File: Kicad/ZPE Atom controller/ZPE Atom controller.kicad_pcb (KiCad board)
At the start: 2 copper layers, 160 x 71.1 mm, 22 parts, among them IC1 TC4424AVPA, P1 CONN_01X18, P2 CONN_01X18, Q1 PN2222A, T1 Transformer_SP_1S, U1 SSD1306, U2 LM7805_TO220

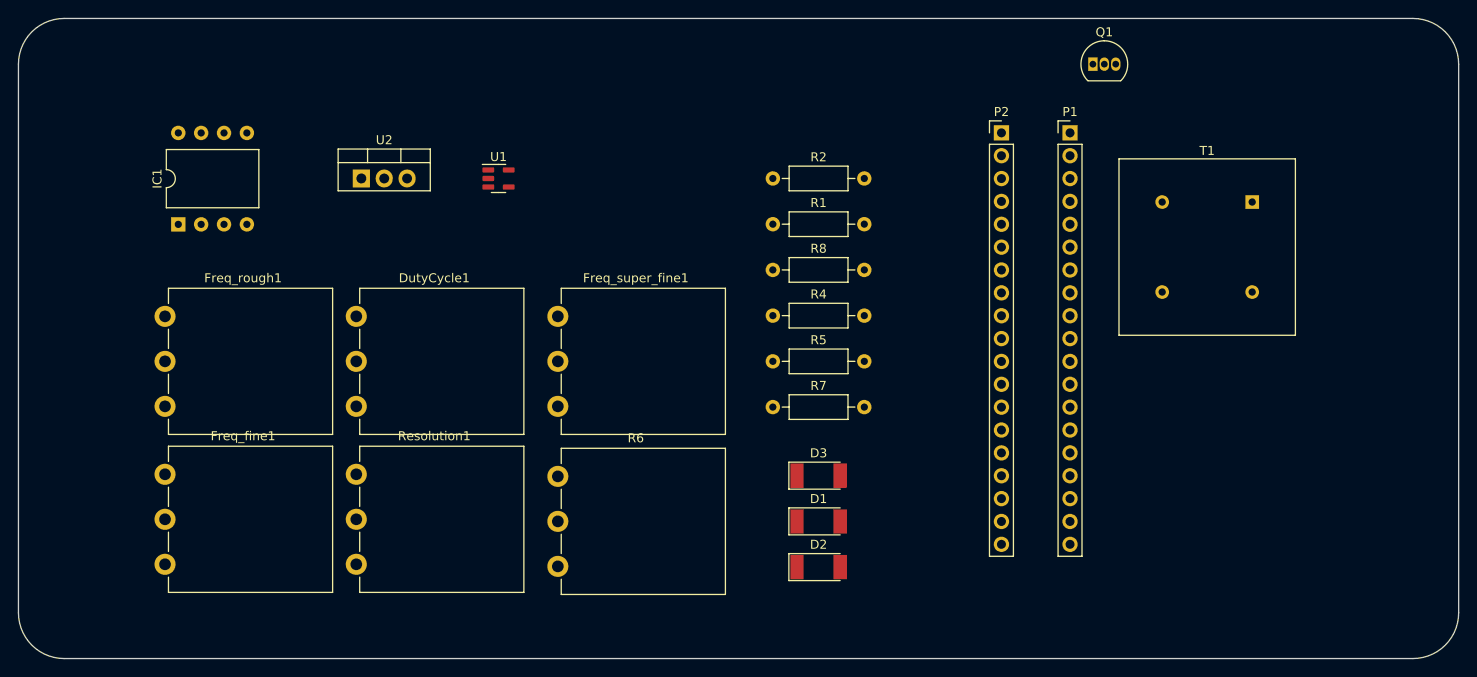
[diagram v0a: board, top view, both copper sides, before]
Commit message: Added AC level convert on inputs
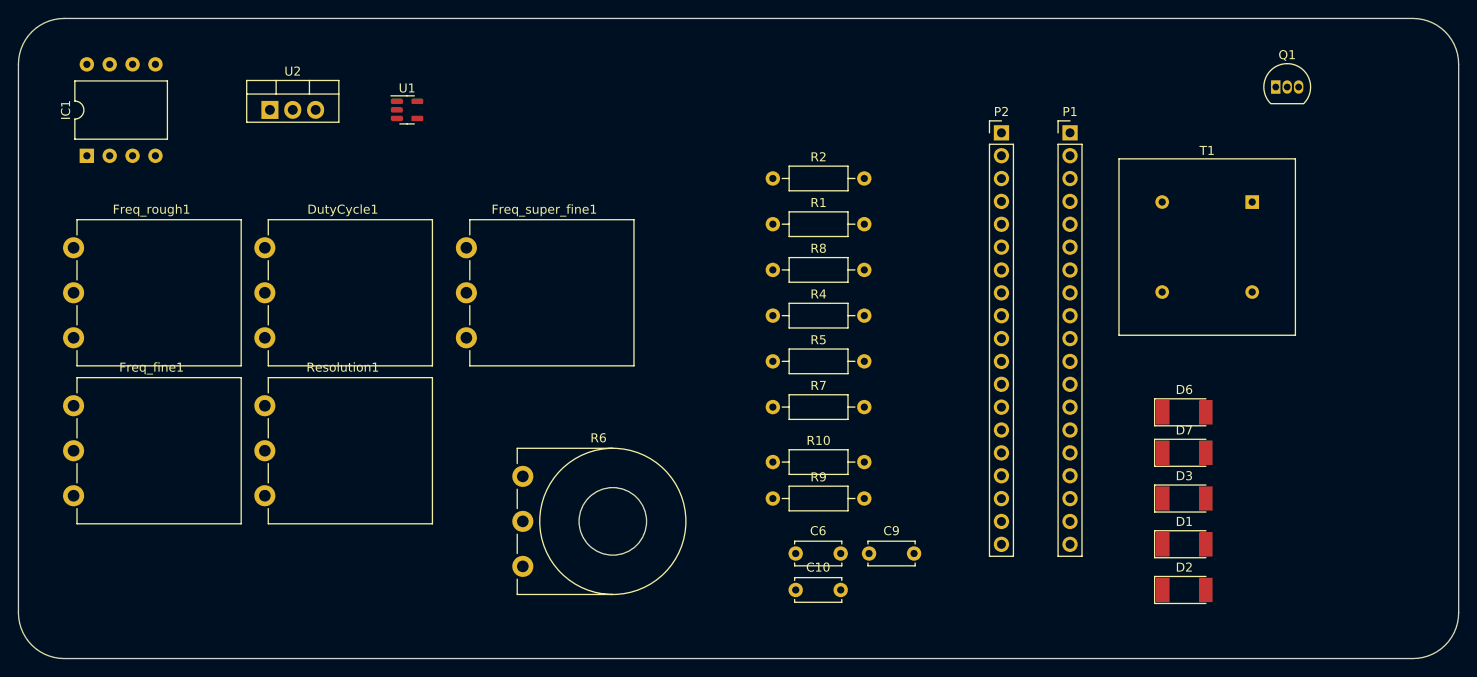
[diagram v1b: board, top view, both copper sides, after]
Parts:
- added C10: 10nF, Capacitor_THT:C_Disc_D5.0mm_W2.5mm_P5.00mm, F.Cu at (154.9, 124.5)
- added C6: 1NF 400V, Capacitor_THT:C_Disc_D5.0mm_W2.5mm_P5.00mm, F.Cu at (154.9, 120.4)
- added C9: 10nF, Capacitor_THT:C_Disc_D5.0mm_W2.5mm_P5.00mm, F.Cu at (163.1, 120.4)
- added D6: 4004, Diode_SMD:D_MELF, F.Cu at (198.1, 104.7)
- added D7: 4004, Diode_SMD:D_MELF, F.Cu at (198.1, 109.2)
- added R10: 1M, Resistor_THT:R_Axial_DIN0207_L6.3mm_D2.5mm_P10.16mm_Horizontal, F.Cu at (152.4, 110.2)
- added R9: 1M, Resistor_THT:R_Axial_DIN0207_L6.3mm_D2.5mm_P10.16mm_Horizontal, F.Cu at (152.4, 114.3)
- R5: value 1k -> 1M
- R6: footprint Potentiometer_THT:Potentiometer_Piher_PC-16_Single_Vertical -> Potentiometer_THT:Potentiometer_Piher_T-16L_Single_Vertical_Hole
- moved D1 40.7 mm to (198.1, 119.4)
- moved D2 40.7 mm to (198.1, 124.5)
- moved D3 40.7 mm to (198.1, 114.3)
- moved Q1 20.5 mm to (208.3, 68.6)
- moved DutyCycle1 12.7 mm to (96.0, 96.4)
- moved Freq_fine1 12.7 mm to (74.7, 114.0)
- moved Freq_rough1 12.7 mm to (74.7, 96.4)
- moved Resolution1 12.7 mm to (96.0, 114.0)
- moved U2 12.7 mm to (96.5, 71.1)
- moved Freq_super_fine1 12.7 mm to (118.3, 96.4)
- moved IC1 12.7 mm to (76.2, 76.2)
- moved U1 12.7 mm to (111.8, 71.1)
- moved R6 3.89 mm to (124.6, 121.8)
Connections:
- R4 pad 1: Net-(D2-K) -> Net-(R4-Pad1)
- R5 pad 1: GND -> Net-(R5-Pad1)
- R5 pad 2: Net-(D2-K) -> Net-(R4-Pad1)
- R7 pad 2: /IO15 -> /IO17

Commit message: Changed pins for feedback to prin 18 and 19
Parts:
- removed R10, R4: 1M, Resistor_THT:R_Axial_DIN0207_L6.3mm_D2.5mm_P10.16mm_Horizontal
- removed U2: LM7805_TO220, Package_TO_SOT_THT:TO-220-3_Vertical
- R5: value 1M -> 1K
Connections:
- C10 pad 1: Net-(R4-Pad1) -> /IO18
- C10 pad 2: Net-(R5-Pad1) -> GND
- C9 pad 1: Net-(D6-K) -> /IO19
- D6 pad 1: Net-(D6-K) -> /IO19
- D7 pad 1: Net-(R4-Pad1) -> /IO18
- R5 pad 1: Net-(R5-Pad1) -> GND
- R5 pad 2: Net-(R4-Pad1) -> /IO18
- R7 pad 1: Net-(D6-K) -> Net-(D5-Pad4)
- R7 pad 2: /IO17 -> Net-(D6-A)
- R8 pad 2: Net-(D6-K) -> /IO19

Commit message: Added caps to inputs of the pots.
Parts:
- added C11: 100nF, Capacitor_THT:C_Disc_D5.0mm_W2.5mm_P5.00mm, F.Cu at (121.9, 74.9)
- added C12: 100nF, Capacitor_THT:C_Disc_D5.0mm_W2.5mm_P5.00mm, F.Cu at (121.9, 70.9)
- added C13: 100nF, Capacitor_THT:C_Disc_D5.0mm_W2.5mm_P5.00mm, F.Cu at (130.1, 70.9)
- added C14: 100nF, Capacitor_THT:C_Disc_D5.0mm_W2.5mm_P5.00mm, F.Cu at (138.2, 70.9)
- added C15: 100nF, Capacitor_THT:C_Disc_D5.0mm_W2.5mm_P5.00mm, F.Cu at (138.2, 74.9)
- C10, C9: value 10nF -> 100nF
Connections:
- C10 pad 1: /IO18 -> /IO12
- C9 pad 1: /IO19 -> /IO14
- D6 pad 1: /IO19 -> /IO14
- D7 pad 1: /IO18 -> /IO12
- R5 pad 2: /IO18 -> /IO12
- R8 pad 2: /IO19 -> /IO14
